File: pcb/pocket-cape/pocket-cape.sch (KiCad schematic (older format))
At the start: 33 parts, among them J1 Sync1, J2 12..16V, J3 Sync2, J4 Sled, J5 Laser1, J6 PM1, J7 PM2, J8 Laser2, U1 MIC920, U2 74LVC2G14GV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

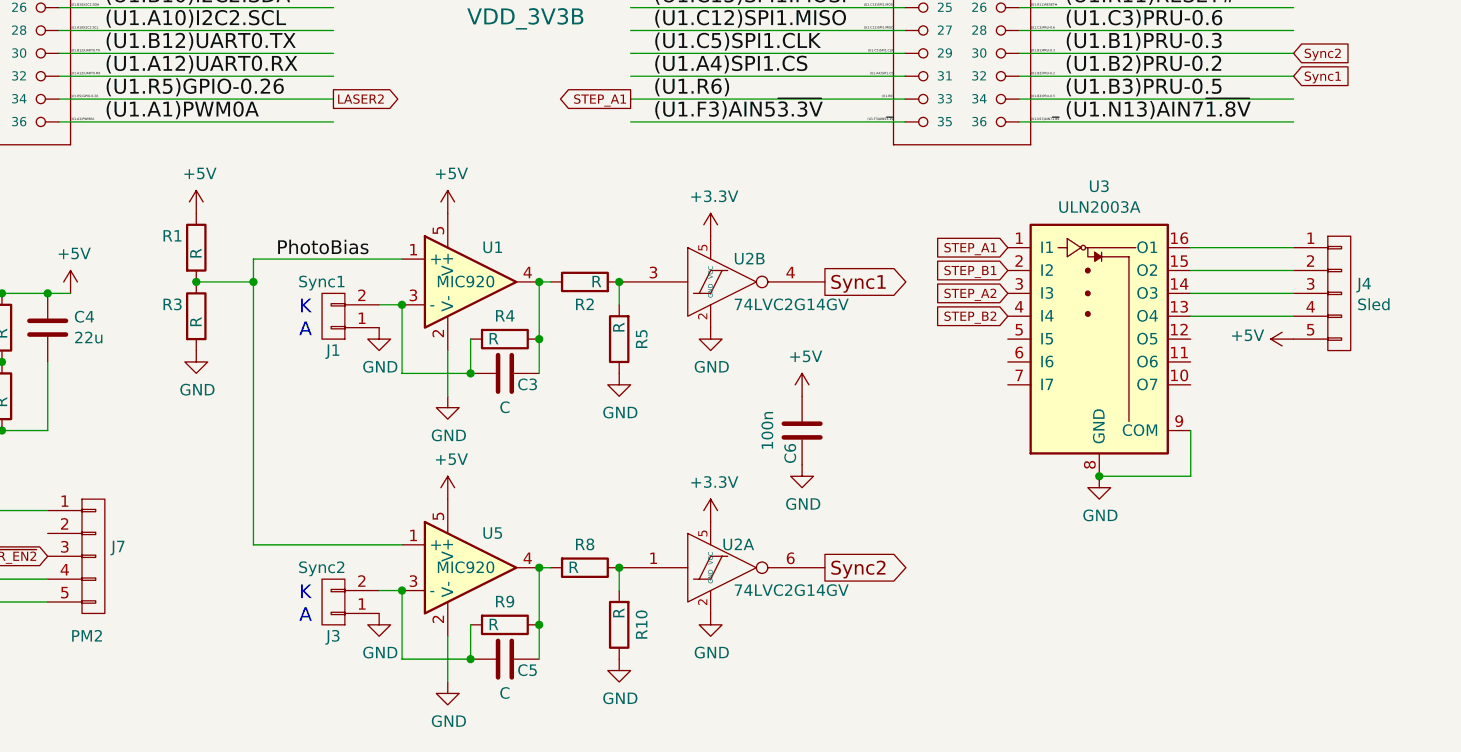
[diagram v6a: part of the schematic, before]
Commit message: Simplyfy photo diode sync input.
o The 74LVC14 inputs are sufficiently high impedance that we
  can directly connect the photo input.
o Also: switch to JST PH 2mm connectors for laser output.
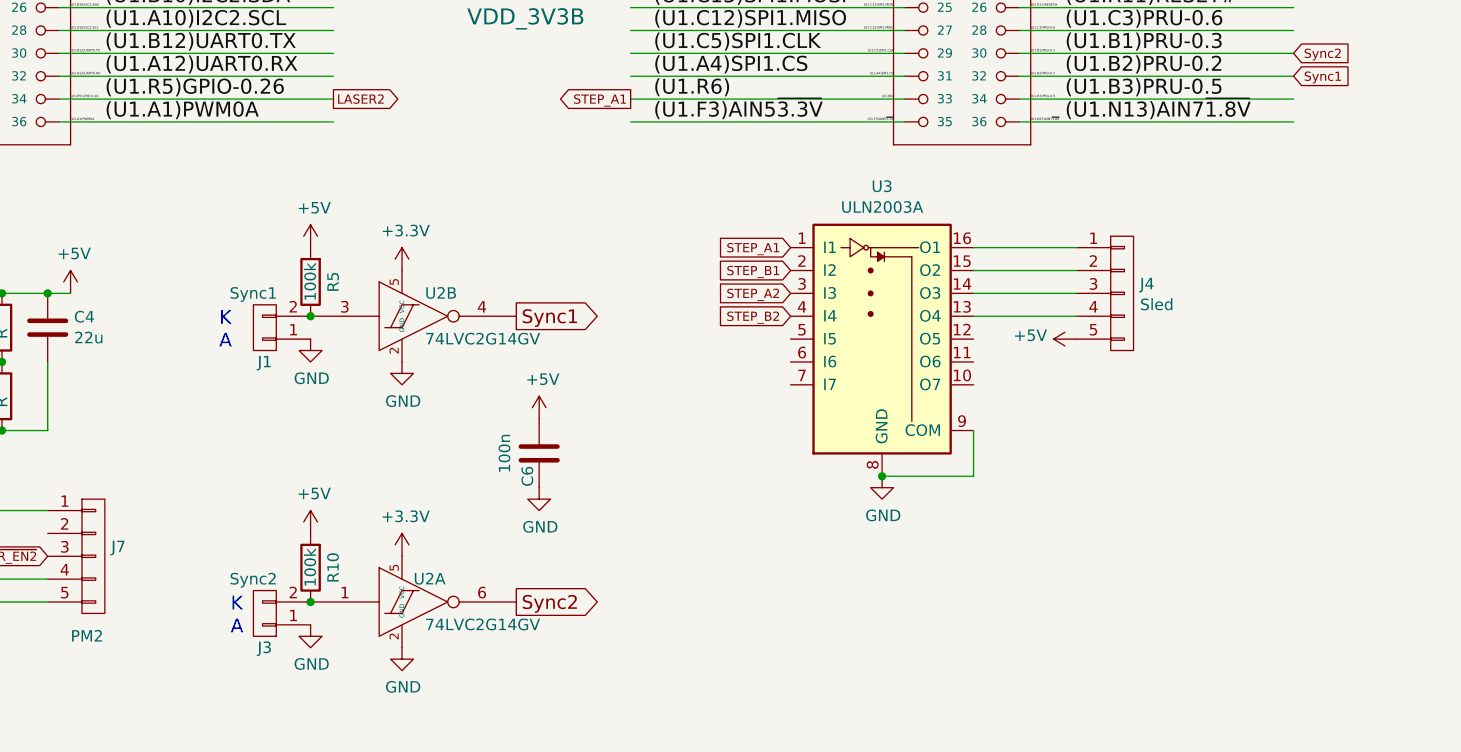
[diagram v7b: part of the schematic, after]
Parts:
- removed C3, C5: C, Capacitors_SMD:C_0603, symbol C
- removed R1, R2, R3, R4, R8, R9: R, Resistors_SMD:R_0603, symbol R
- removed U1, U5: MIC920, TO_SOT_Packages_SMD:SOT-23-5, symbol MIC920
- J5, J8: footprint Connectors_JST:JST_XH_B03B-XH-A_03x2.50mm_Straight -> Connectors_JST:JST_PH_B3B-PH-K_03x2.00mm_Straight
- R10, R5: value R -> 100k
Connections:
- net labels removed: PhotoBias
- wire segments 113 -> 93
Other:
- moved on the sheet: C6, J1, J3, J4, R10, R5, U2A, U2B, U3

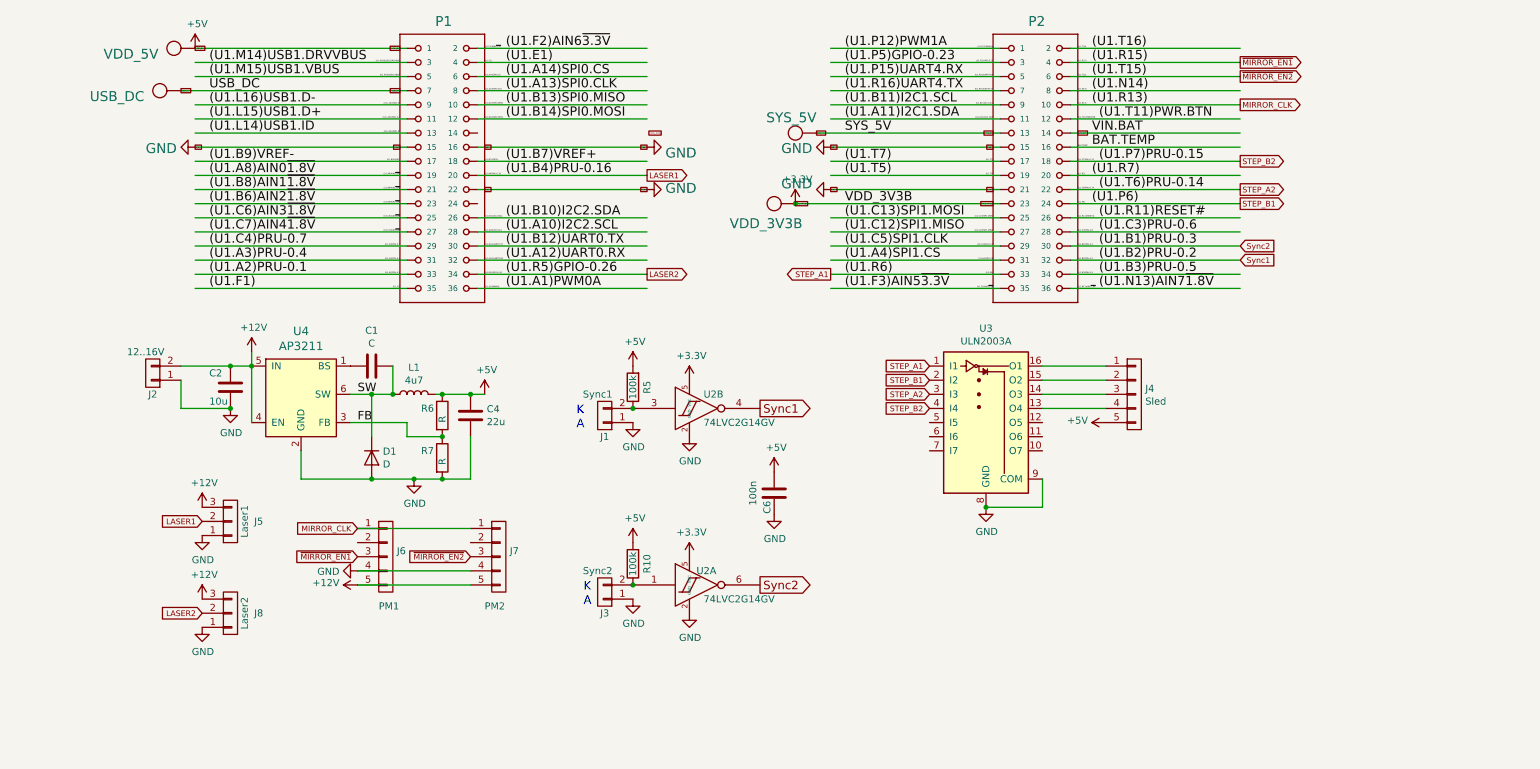
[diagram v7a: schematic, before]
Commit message: Intermediate state: initial display and USB connector.
o Add flat flex connector to drive a simple SPI-based display.
o Try to cram a vertial USB connector onto the board to be able
  to have a wifi dongle.
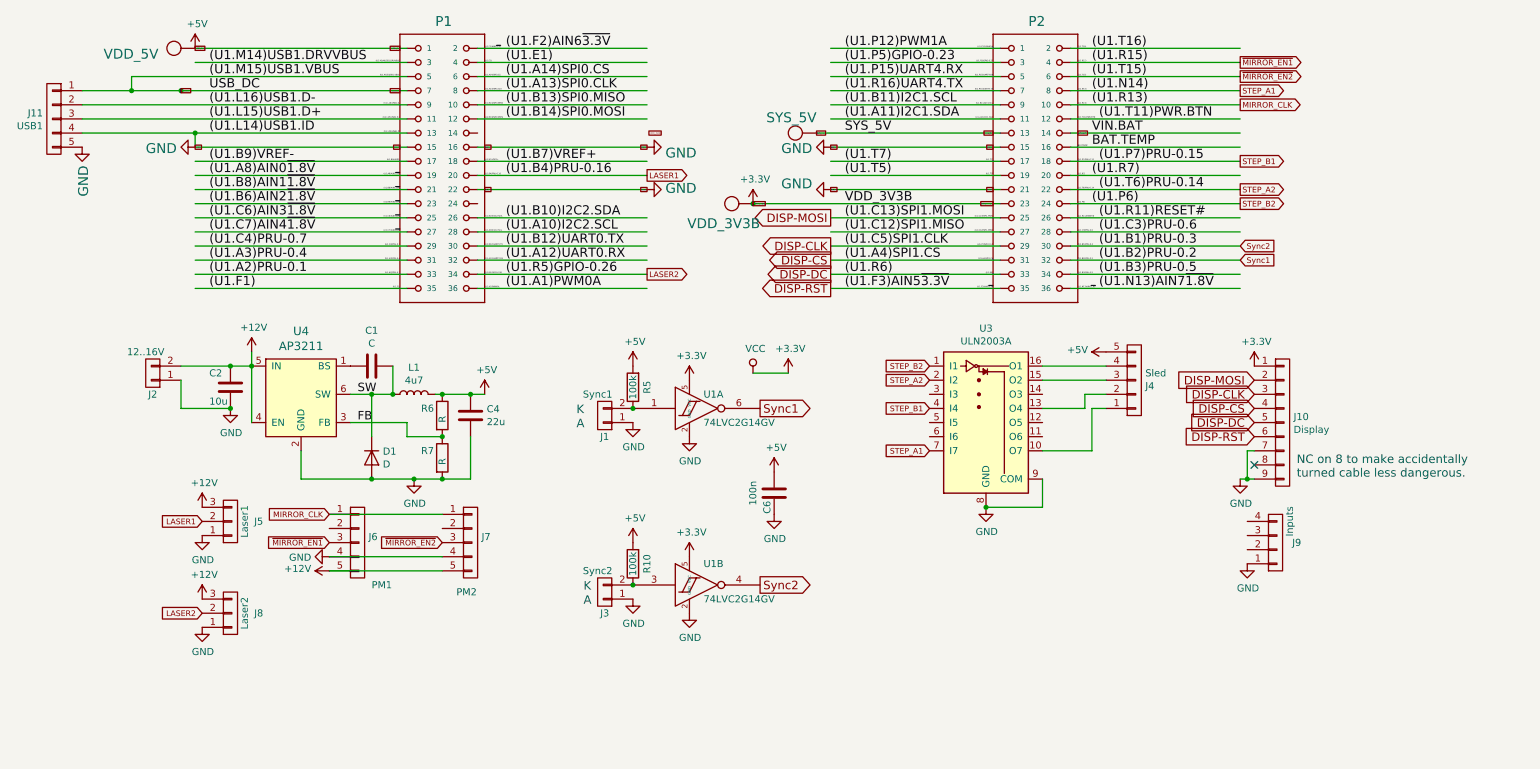
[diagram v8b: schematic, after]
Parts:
- removed U2: 74LVC2G14GV, TO_SOT_Packages_SMD:TSOT-23-6_MK06A, symbol 74LVC2G14GV
- added J10: Display, ldgraphy.pretty:FlatFlexConn-08, symbol CONN_01X09
- added J11: USB1, ldgraphy.pretty:USB-A-Vertical, symbol CONN_01X05
- added J9: Inputs, Connectors_JST:JST_PH_B4B-PH-K_04x2.00mm_Straight, symbol CONN_01X04
- added U1: 74LVC2G14GV, TO_SOT_Packages_SMD:SOT-23-6, symbol 74LVC2G14GV
- J1, J3: footprint Connectors_JST:JST_PH_S2B-PH-K_02x2.00mm_Angled -> Connectors_JST:JST_PH_B2B-PH-K_02x2.00mm_Straight
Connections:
- net labels added: DISP-CLK, DISP-CS, DISP-DC, DISP-MOSI, DISP-RST, VCC
- wire segments 93 -> 103
- no-connect marks 0 -> 1
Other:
- note added: "NC on 8 to make accidentally\nturned cable less dangerous."
- moved on the sheet: J4, J6, J7
